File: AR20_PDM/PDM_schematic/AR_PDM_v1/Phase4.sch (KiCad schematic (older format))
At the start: 15 parts, among them Q1 BTS50025-1TAD, U1 INA233

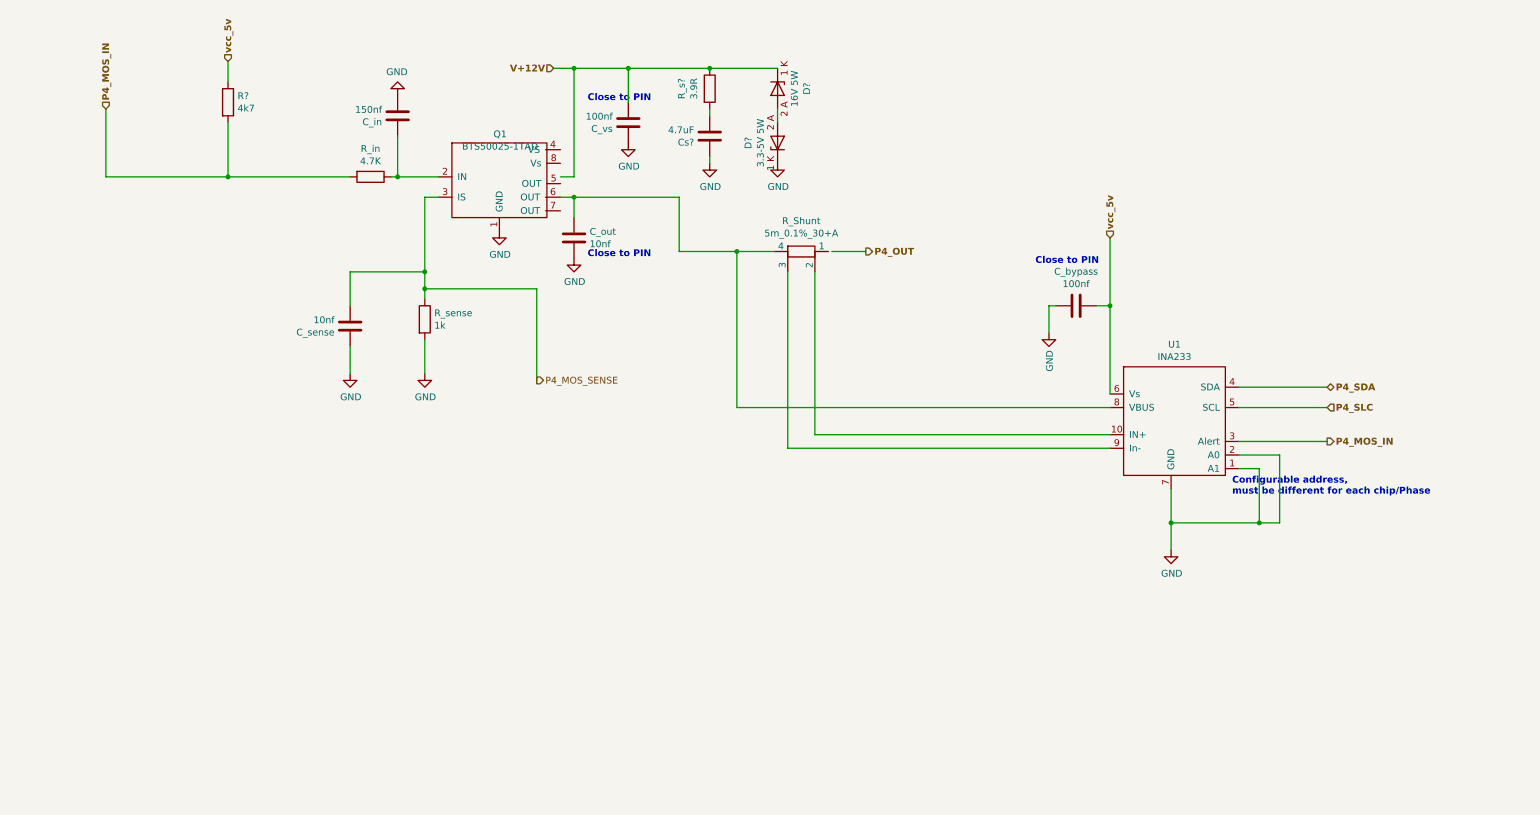
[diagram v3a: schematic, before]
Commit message: Fixed issues, controlled components, BOM, see discription
- added acm symbol
- fixed wrongly faced P-mosfets
- I/O expander now sinks led instead of source
- Bill of material mostly done
- Correct address for INA233 chips.
- Now 4 diodes serves as flyback for all mosfets
- Corrected naming scheme for compmonents (everything is not fixed yet)
- Fixed some labels
- altso some minor changes
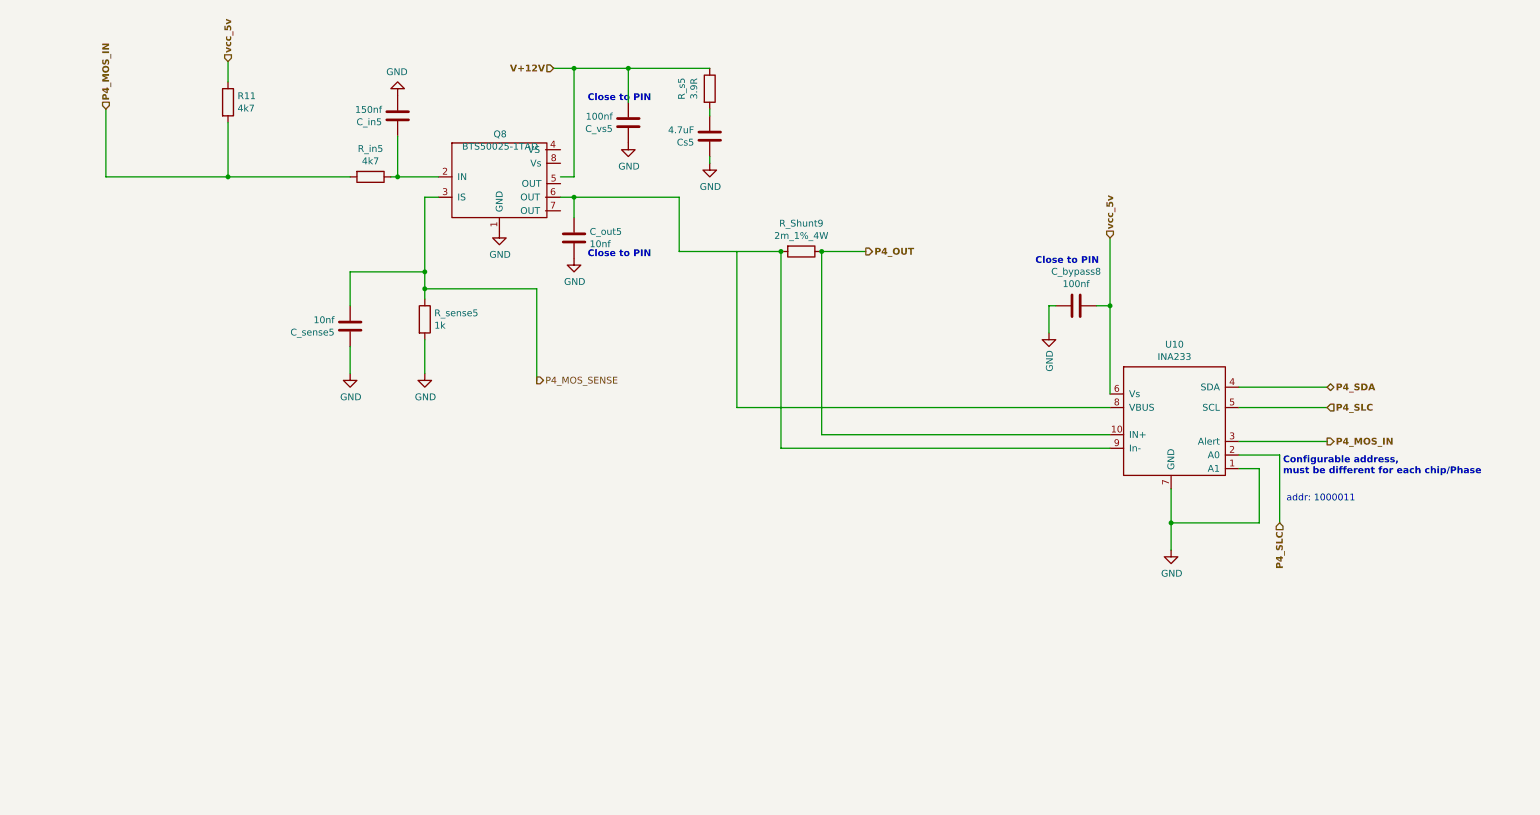
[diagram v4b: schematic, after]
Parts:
- removed C_bypass, C_vs: 100nf, symbol AR20_PDM_v1-rescue:C-Device
- removed C_in: 150nf, symbol AR20_PDM_v1-rescue:C-Device
- removed C_out: 10nf, symbol AR20_PDM_v1-rescue:C-Device
- removed D?: 3.3-5V 5W, symbol AR20_PDM_v1-rescue:D_Zener-Device
- removed D?: 16V 5W, symbol AR20_PDM_v1-rescue:D_Zener-Device
- removed Q1: BTS50025-1TAD, symbol AR20_PDM_v1-rescue:BTS50025-1TAD
- removed R?: 4k7, symbol AR20_PDM_v1-rescue:R-Device
- removed R_Shunt: 5m_0.1%_30+A, symbol AR20_PDM_v1-rescue:R_Shunt-Device
- removed R_in: 4.7K, symbol AR20_PDM_v1-rescue:R-Device
- removed R_s?: 3.9R, symbol AR20_PDM_v1-rescue:R-Device
- removed R_sense: 1k, symbol AR20_PDM_v1-rescue:R-Device
- removed U1: INA233, symbol AR20_PDM_v1-rescue:INA233
- added C_bypass8, C_vs5: 100nf, Capacitor_SMD:C_0603_1608Metric, symbol AR20_PDM_v1-rescue:C-Device
- added C_in5: 150nf, Capacitor_SMD:C_0603_1608Metric, symbol AR20_PDM_v1-rescue:C-Device
- added C_out5: 10nf, Capacitor_SMD:C_0603_1608Metric, symbol AR20_PDM_v1-rescue:C-Device
- added Q8: BTS50025-1TAD, symbol AR20_PDM_v1-rescue:BTS50025-1TAD
- added R11, R_in5: 4k7, symbol AR20_PDM_v1-rescue:R-Device
- added R_Shunt9: 2m_1%_4W, symbol AR20_PDM_v1-rescue:R-Device
- added R_s5: 3.9R, symbol AR20_PDM_v1-rescue:R-Device
- added R_sense5: 1k, symbol AR20_PDM_v1-rescue:R-Device
- added U10: INA233, symbol AR20_PDM_v1-rescue:INA233
- C_sense5: renamed from C_sense; footprint (none) -> Capacitor_SMD:C_0603_1608Metric
- Cs5: renamed from Cs?; footprint (none) -> Capacitor_SMD:C_1206_3216Metric
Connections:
- wire segments 57 -> 54
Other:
- note added: "addr: 1000011"

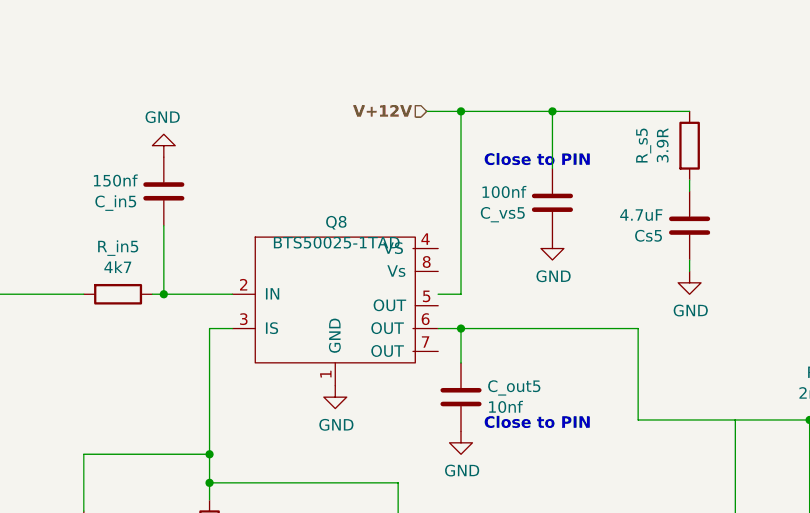
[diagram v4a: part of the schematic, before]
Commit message: PCB design, and issue fixing, work in progress
- Error fixed: Mux mosfet resistor change to ground
- Open drain output added on phase 6, for engine blipping purpose
- Most of pcb symbols and footprints are finished, including main connector
- PCB is change from 1oz to 2oz copper layer, for easier routing.
- Basic Draft of pcb is done, for now.
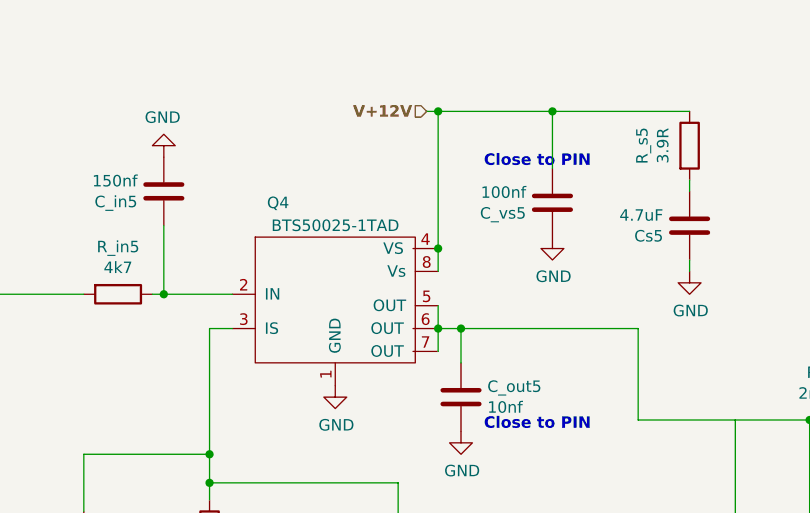
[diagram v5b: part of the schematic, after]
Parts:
- Q4: renamed from Q8; footprint (none) -> AR_PDM_v1:BTS500xx
- R11, R_in5, R_s5, R_sense5: footprint (none) -> Resistor_SMD:R_0603_1608Metric
- R_Shunt9: footprint (none) -> Resistor_SMD:R_2512_6332Metric
- U10: footprint (none) -> AR_PDM_v1:INA233
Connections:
- net V+12V: now also Q4.4 (VS), Q4.8 (Vs)
- net at C_out5.1, Q4.6 (OUT), R_Shunt9.2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: now also Q4.5 (OUT), Q4.7 (OUT)
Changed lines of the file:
@@
 F 0 "R_in5" V 3093 2400 50  0000 C CNN
 F 1 "4k7" V 3184 2400 50  0000 C CNN
-F 2 "" V 3230 2400 50  0001 C CNN
+F 2 "Resistor_SMD:R_0603_1608Metric" V 3230 2400 50  0001 C CNN
 F 3 "~" H 3300 2400 50  0001 C CNN
 	1    3300 2400
@@
 F 0 "R11" H 2320 1896 50  0000 L CNN
 F 1 "4k7" H 2320 1805 50  0000 L CNN
-F 2 "" V 2180 1850 50  0001 C CNN
+F 2 "Resistor_SMD:R_0603_1608Metric" V 2180 1850 50  0001 C CNN
 F 3 "~" H 2250 1850 50  0001 C CNN
 	1    2250 1850
@@
 AR Path="/5E0FB5C8/5E21B7FA" Ref="Q?"  Part="1"
 AR Path="/5E0FBBBD/5E21B7FA" Ref="Q?"  Part="1"
-AR Path="/5E0FC3A2/5E21B7FA" Ref="Q8"  Part="1"
+AR Path="/5E0FC3A2/5E21B7FA" Ref="Q4"  Part="1"
 AR Path="/5E0FCFDC/5E21B7FA" Ref="Q?"  Part="1"
 AR Path="/5E0FDCCC/5E21B7FA" Ref="Q?"  Part="1"
 AR Path="/5E10174B/5E21B7FA" Ref="Q?"  Part="1"
-F 0 "Q8" H 4255 3215 50  0000 C CNN
-F 1 "BTS50025-1TAD" H 4255 3124 50  0000 C CNN
-F 2 "" H 4250 2650 50  0001 C CNN
+F 0 "Q4" H 4000 3300 50  0000 C CNN
+F 1 "BTS50025-1TAD" H 4250 3200 50  0000 C CNN
+F 2 "AR_PDM_v1:BTS500xx" H 4250 2650 50  0001 C CNN
 F 3 "" H 4250 2650 50  0001 C CNN
 	1    4250 2650
@@
 F 0 "U10" H 9225 4465 50  0000 C CNN
 F 1 "INA233" H 9225 4374 50  0000 C CNN
-F 2 "" H 9200 4050 50  0001 C CNN
+F 2 "AR_PDM_v1:INA233" H 9200 4050 50  0001 C CNN
 F 3 "" H 9200 4050 50  0001 C CNN
 	1    9200 4050
@@
 Wire Wire Line
 	3700 3100 3700 3225
-Wire Wire Line
-	4700 2400 4800 2400
-Wire Wire Line
-	4800 2400 4800 1600
-Wire Wire Line
-	4800 1600 4650 1600
 Text HLabel 2250 1550 1    50   Input ~ 10
 vcc_5v
@@
 F 0 "R_s5" V 5593 1750 50  0000 C CNN
 F 1 "3.9R" V 5684 1750 50  0000 C CNN
-F 2 "" V 5730 1750 50  0001 C CNN
+F 2 "Resistor_SMD:R_0603_1608Metric" V 5730 1750 50  0001 C CNN
 F 3 "~" H 5800 1750 50  0001 C CNN
 	1    5800 1750
@@
 Wire Wire Line
 	5200 1600 5800 1600
-Wire Wire Line
-	4800 1600 5200 1600
-Connection ~ 4800 1600
 Connection ~ 5200 1600
 Text HLabel 1350 1900 1    50   Input ~ 10
@@
 F 0 "R_sense5" H 3770 3496 50  0000 L CNN
 F 1 "1k" H 3770 3405 50  0000 L CNN
-F 2 "" V 3630 3450 50  0001 C CNN
+F 2 "Resistor_SMD:R_0603_1608Metric" V 3630 3450 50  0001 C CNN
 F 3 "~" H 3700 3450 50  0001 C CNN
 	1    3700 3450
@@
 F 0 "R_Shunt9" V 6268 2950 50  0000 C CNN
 F 1 "2m_1%_4W" V 6359 2950 50  0000 C CNN
-F 2 "" V 6405 2950 50  0001 C CNN
+F 2 "Resistor_SMD:R_2512_6332Metric" V 6405 2950 50  0001 C CNN
 F 3 "~" H 6475 2950 50  0001 C CNN
 	1    6475 2950
@@
 Text HLabel 10000 4950 3    50   Input ~ 10
 P4_SLC
+Wire Wire Line
+	4700 2550 4700 2650
+Connection ~ 4700 2550
+Wire Wire Line
+	4700 2550 4700 2450
+Wire Wire Line
+	4650 1600 4700 1600
+Wire Wire Line
+	4700 2300 4700 2200
+Wire Wire Line
+	4700 2200 4700 1600
+Connection ~ 4700 2200
+Connection ~ 4700 1600
+Wire Wire Line
+	4700 1600 5200 1600
 $EndSCHEMATC

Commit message: PCB Design, Work in progress
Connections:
- net P4_Shunt: now reaches C_out5.1, Q4.5 (OUT), Q4.6 (OUT), Q4.7 (OUT), R_Shunt9.2, U10.8 (VBUS), U10.9 (In-)
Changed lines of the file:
@@
 $Descr A4 11693 8268
 encoding utf-8
-Sheet 9 13
+Sheet 8 13
 Title ""
 Date ""
@@
 Wire Wire Line
 	4700 1600 5200 1600
+Wire Wire Line
+	6000 2950 6000 2825
+Text HLabel 6000 2825 1    50   Input ~ 0
+P4_Shunt
+Connection ~ 6000 2950
 $EndSCHEMATC

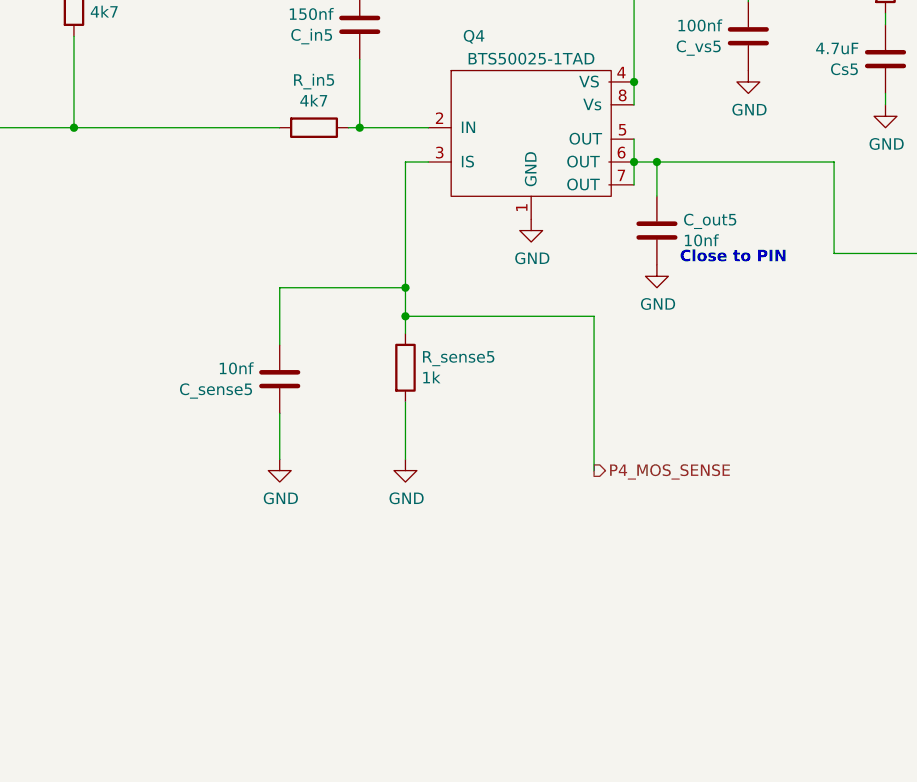
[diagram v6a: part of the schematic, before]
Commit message: PCB Design,  minor schematics changes, work in progress, see description
- Removed mos sense caps and resistors accept one, 
since only one measurement can be done, at a time.
- added mos sens protection resistors on each line, to protect mux mosfets and micro controller. 
- Routing plan mostly finalized, some of the traces are just proof of concept.
those needs to be routed nicely.
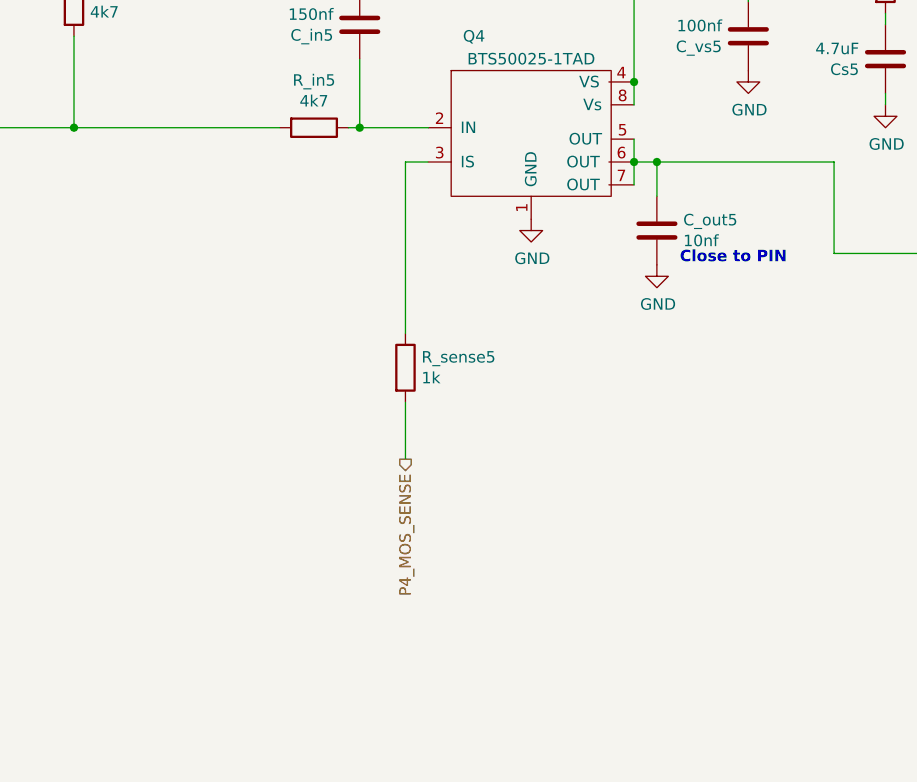
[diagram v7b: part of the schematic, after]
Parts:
- removed C_sense5: 10nf, Capacitor_SMD:C_0603_1608Metric, symbol AR20_PDM_v1-rescue:C-Device
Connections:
- net GND: no longer R_sense5.2
- net P4_MOS_SENSE: now also R_sense5.2; no longer Q4.3 (IS), R_sense5.1
- new net: Q4.3 (IS), R_sense5.1
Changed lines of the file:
@@
-	1    0    0    -1
-$EndComp
-$Comp
-L AR20_PDM_v1-rescue:GND-power #PWR?
-U 1 1 5E21B822
-P 3700 3850
-AR Path="/5DA89415/5E21B822" Ref="#PWR?"  Part="1"
-AR Path="/5DEB10A1/5E21B822" Ref="#PWR?"  Part="1"
-AR Path="/5DEB20EA/5E21B822" Ref="#PWR?"  Part="1"
-AR Path="/5E0E4725/5E21B822" Ref="#PWR?"  Part="1"
-AR Path="/5E0E4A93/5E21B822" Ref="#PWR?"  Part="1"
-AR Path="/5E0E4EB5/5E21B822" Ref="#PWR?"  Part="1"
-AR Path="/5E0E5304/5E21B822" Ref="#PWR?"  Part="1"
-AR Path="/5E0E594B/5E21B822" Ref="#PWR?"  Part="1"
-AR Path="/5E0E607C/5E21B822" Ref="#PWR?"  Part="1"
-AR Path="/5E0FB5C8/5E21B822" Ref="#PWR?"  Part="1"
-AR Path="/5E0FBBBD/5E21B822" Ref="#PWR?"  Part="1"
-AR Path="/5E0FC3A2/5E21B822" Ref="#PWR074"  Part="1"
-AR Path="/5E0FCFDC/5E21B822" Ref="#PWR?"  Part="1"
-AR Path="/5E0FDCCC/5E21B822" Ref="#PWR?"  Part="1"
-AR Path="/5E10174B/5E21B822" Ref="#PWR?"  Part="1"
-F 0 "#PWR074" H 3700 3600 50  0001 C CNN
-F 1 "GND" H 3705 3677 50  0000 C CNN
-F 2 "" H 3700 3850 50  0001 C CNN
-F 3 "" H 3700 3850 50  0001 C CNN
-	1    3700 3850
 	1    0    0    -1
 $EndComp
@@
 $EndComp
 Wire Wire Line
-	3700 2550 3700 3100
-Wire Wire Line
 	3700 2550 3800 2550
-Wire Wire Line
-	3700 3850 3700 3600
 Wire Wire Line
 	8750 2850 8750 3350
@@
 Wire Wire Line
 	9700 4450 10000 4450
-$Comp
-L AR20_PDM_v1-rescue:GND-power #PWR?
-U 1 1 5E21B84A
-P 3150 3850
-AR Path="/5DA89415/5E21B84A" Ref="#PWR?"  Part="1"
-AR Path="/5DEB10A1/5E21B84A" Ref="#PWR?"  Part="1"
-AR Path="/5DEB20EA/5E21B84A" Ref="#PWR?"  Part="1"
-AR Path="/5E0E4725/5E21B84A" Ref="#PWR?"  Part="1"
-AR Path="/5E0E4A93/5E21B84A" Ref="#PWR?"  Part="1"
-AR Path="/5E0E4EB5/5E21B84A" Ref="#PWR?"  Part="1"
-AR Path="/5E0E5304/5E21B84A" Ref="#PWR?"  Part="1"
-AR Path="/5E0E594B/5E21B84A" Ref="#PWR?"  Part="1"
-AR Path="/5E0E607C/5E21B84A" Ref="#PWR?"  Part="1"
-AR Path="/5E0FB5C8/5E21B84A" Ref="#PWR?"  Part="1"
-AR Path="/5E0FBBBD/5E21B84A" Ref="#PWR?"  Part="1"
-AR Path="/5E0FC3A2/5E21B84A" Ref="#PWR072"  Part="1"
-AR Path="/5E0FCFDC/5E21B84A" Ref="#PWR?"  Part="1"
-AR Path="/5E0FDCCC/5E21B84A" Ref="#PWR?"  Part="1"
-AR Path="/5E10174B/5E21B84A" Ref="#PWR?"  Part="1"
-F 0 "#PWR072" H 3150 3600 50  0001 C CNN
-F 1 "GND" H 3155 3677 50  0000 C CNN
-F 2 "" H 3150 3850 50  0001 C CNN
-F 3 "" H 3150 3850 50  0001 C CNN
-	1    3150 3850
-	1    0    0    -1
-$EndComp
-$Comp
-L AR20_PDM_v1-rescue:C-Device C_sense?
-U 1 1 5DAAC283
-P 3150 3500
-AR Path="/5DA89415/5DAAC283" Ref="C_sense?"  Part="1"
-AR Path="/5DEB10A1/5DAAC283" Ref="C_sense?"  Part="1"
-AR Path="/5DEB20EA/5DAAC283" Ref="C_sense?"  Part="1"
-AR Path="/5E0E4725/5DAAC283" Ref="C_sense?"  Part="1"
-AR Path="/5E0E4A93/5DAAC283" Ref="C_sense?"  Part="1"
-AR Path="/5E0E4EB5/5DAAC283" Ref="C_sense?"  Part="1"
-AR Path="/5E0E5304/5DAAC283" Ref="C_sense?"  Part="1"
-AR Path="/5E0E594B/5DAAC283" Ref="C_sense?"  Part="1"
-AR Path="/5E0E607C/5DAAC283" Ref="C_sense?"  Part="1"
-AR Path="/5E0FB5C8/5DAAC283" Ref="C_sense?"  Part="1"
-AR Path="/5E0FBBBD/5DAAC283" Ref="C_sense?"  Part="1"
-AR Path="/5E0FC3A2/5DAAC283" Ref="C_sense5"  Part="1"
-AR Path="/5E0FCFDC/5DAAC283" Ref="C_sense?"  Part="1"
-AR Path="/5E0FDCCC/5DAAC283" Ref="C_sense?"  Part="1"
-AR Path="/5E10174B/5DAAC283" Ref="C_sense?"  Part="1"
-F 0 "C_sense5" H 3265 3546 50  0000 L CNN
-F 1 "10nf" H 3265 3455 50  0000 L CNN
-F 2 "Capacitor_SMD:C_0603_1608Metric" H 3188 3350 50  0001 C CNN
-F 3 "~" H 3150 3500 50  0001 C CNN
-	1    3150 3500
-	-1   0    0    1
-$EndComp
 Wire Wire Line
 	3450 2400 3500 2400
@@
 Text Notes 8200 3050 0    50   ~ 10
 Close to PIN
-Wire Wire Line
-	3150 3100 3150 3350
-Wire Wire Line
-	3150 3650 3150 3850
-Wire Wire Line
-	3150 3100 3700 3100
-Connection ~ 3700 3100
-Wire Wire Line
-	3700 3100 3700 3225
 Text HLabel 2250 1550 1    50   Input ~ 10
 vcc_5v
@@
 Wire Wire Line
 	6625 4300 8750 4300
-Wire Wire Line
-	3700 3225 4525 3225
-Wire Wire Line
-	4525 3225 4525 3900
-Connection ~ 3700 3225
-Wire Wire Line
-	3700 3225 3700 3300
-Text HLabel 4525 3900 2    50   Output ~ 0
+Text HLabel 3700 3850 3    50   Output ~ 0
 P4_MOS_SENSE
 Wire Wire Line
@@
 P4_Shunt
 Connection ~ 6000 2950
+Wire Wire Line
+	3700 3850 3700 3600
+Wire Wire Line
+	3700 2550 3700 3300
 $EndSCHEMATC
